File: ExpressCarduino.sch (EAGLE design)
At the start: 1 part

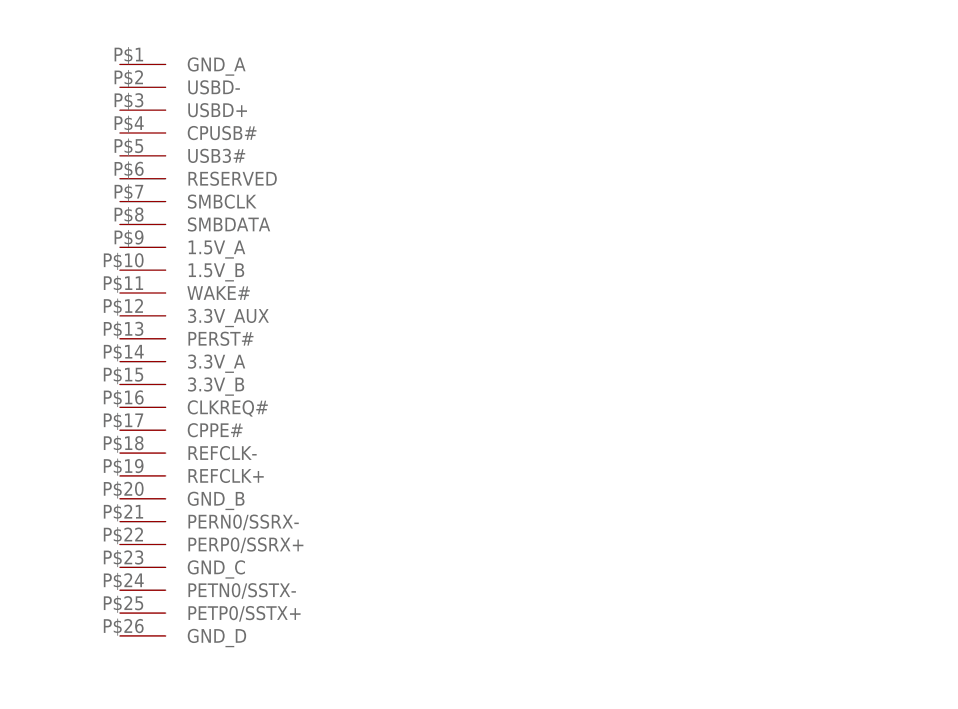
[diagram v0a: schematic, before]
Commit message: Added vreg circuit for 3.3v -> 9v and images
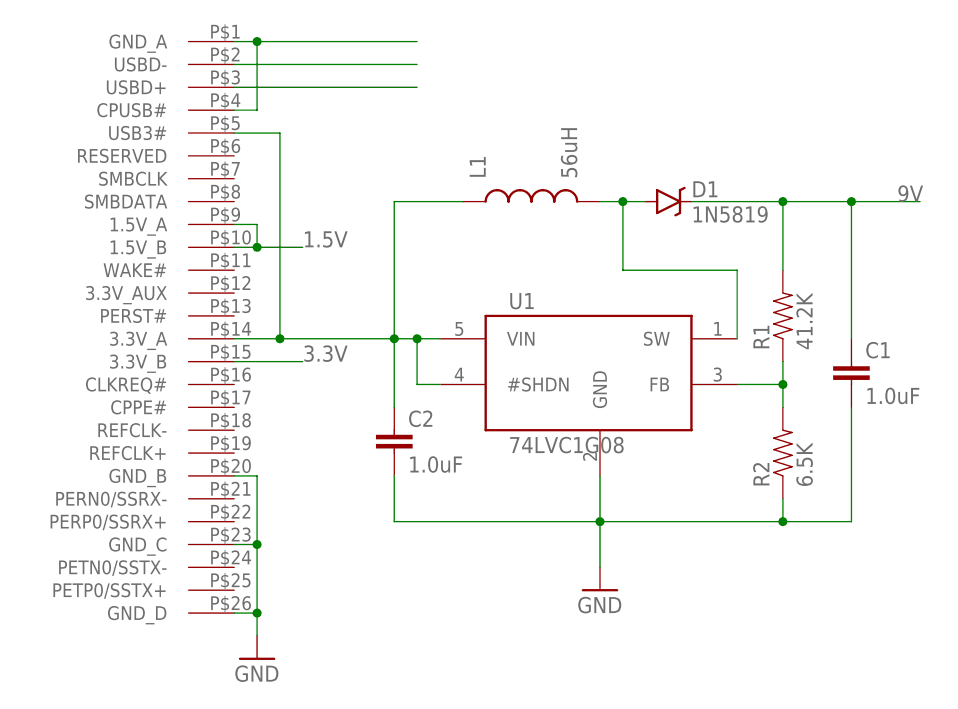
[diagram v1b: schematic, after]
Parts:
- added C1, C2: 1.0uF, SparkFun-Capacitors:1.0UF-16V-10%(0603)
- added D1: 1N5819, HokieGeek:DIODE-SCHOTTKY
- added L1: 56uH, SparkFun-Passives:INDUCTORSDR0403-560KL
- added R1: 41.2K, SparkFun-Resistors:0.22OHM-1/4W-1%(0805)
- added R2: 6.5K, SparkFun-Resistors:0.22OHM-1/4W-1%(0805)
- added U1: 74LVC1G08, HokieGeek:AP3012
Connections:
- new net 1.5V: U$1.1.5V_A, U$1.1.5V_B
- new net 3.3V: U$1.3.3V_B
- new net 9V: C1.1, D1.C, R1.2
- new net GND: C1.2, C2.2, R2.1, U$1.CPUSB#, U$1.GND_A, U$1.GND_B, U$1.GND_C, U$1.GND_D, U1.GND
- new net N$1: R1.1, R2.2, U1.FB
- new net N$2: C2.1, L1.1, U$1.3.3V_A, U$1.USB3#, U1.#SHDN, U1.VIN
- new net N$3: D1.A, L1.2, U1.SW
- new net N$4: U$1.USBD-
- new net N$5: U$1.USBD+

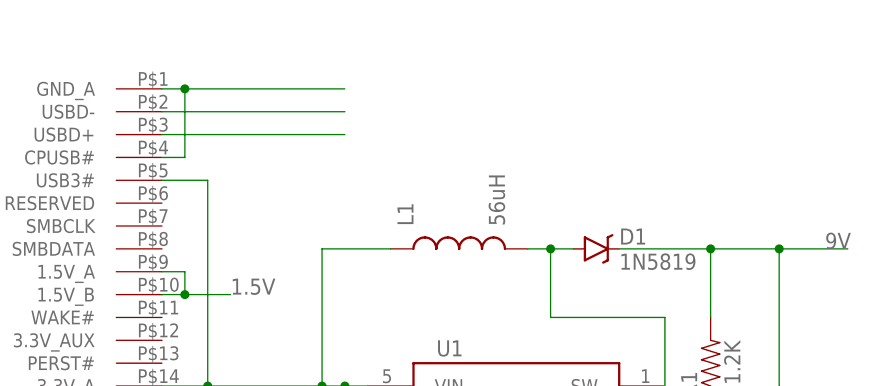
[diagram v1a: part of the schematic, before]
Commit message: Added the Mini USB part
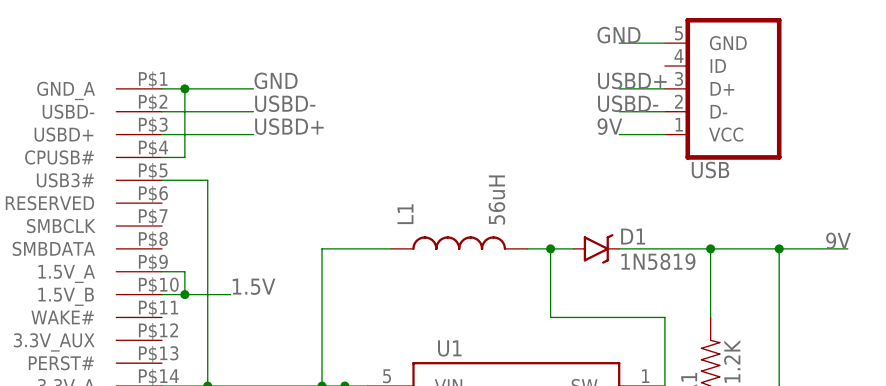
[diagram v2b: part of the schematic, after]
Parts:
- added USB: (no value), HokieGeek:USB_MICROB_PLUG"
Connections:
- removed net N$4: U$1.USBD-
- removed net N$5: U$1.USBD+
- new net USBD+: U$1.USBD+, USB.D+
- new net USBD-: U$1.USBD-, USB.D-
- net 9V: now also USB.VCC
- net GND: now also USB.GND
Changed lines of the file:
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@@
 <part name="L1" library="SparkFun-Passives" deviceset="INDUCTOR" device="SDR0403-560KL" value="56uH"/>
 <part name="D1" library="HokieGeek" deviceset="DIODE-SCHOTTKY" device="" value="1N5819"/>
+<part name="USB" library="HokieGeek" deviceset="USB_MICROB_PLUG" device="&quot;"/>
 </parts>
 <sheets>
@@
 <instance part="L1" gate="G$1" x="48.26" y="50.8" rot="R90"/>
 <instance part="D1" gate="G$1" x="63.5" y="50.8"/>
+<instance part="USB" gate="G$1" x="78.74" y="68.58" rot="MR180"/>
 </instances>
 <busses>
@@
 </segment>
 </net>
-<net name="N$4" class="0">
+<net name="USBD-" class="0">
 <segment>
 <pinref part="U$1" gate="G$1" pin="USBD-"/>
-<wire x1="15.24" y1="66.04" x2="35.56" y2="66.04" width="0.1524" layer="91"/>
+<wire x1="15.24" y1="66.04" x2="25.4" y2="66.04" width="0.1524" layer="91"/>
+<label x="25.4" y="66.04" size="1.778" layer="95"/>
+</segment>
+<segment>
+<pinref part="USB" gate="G$1" pin="D-"/>
+<wire x1="71.12" y1="66.04" x2="66.04" y2="66.04" width="0.1524" layer="91"/>
+<label x="63.5" y="66.04" size="1.778" layer="95"/>
 </segment>
 </net>
-<net name="N$5" class="0">
+<net name="USBD+" class="0">
 <segment>
 <pinref part="U$1" gate="G$1" pin="USBD+"/>
-<wire x1="15.24" y1="63.5" x2="35.56" y2="63.5" width="0.1524" layer="91"/>
+<wire x1="15.24" y1="63.5" x2="25.4" y2="63.5" width="0.1524" layer="91"/>
+<label x="25.4" y="63.5" size="1.778" layer="95"/>
+</segment>
+<segment>
+<pinref part="USB" gate="G$1" pin="D+"/>
+<wire x1="71.12" y1="68.58" x2="66.04" y2="68.58" width="0.1524" layer="91"/>
+<label x="63.5" y="68.58" size="1.778" layer="95"/>
 </segment>
 </net>
@@
 <pinref part="U$1" gate="G$1" pin="GND_A"/>
 <wire x1="15.24" y1="68.58" x2="17.78" y2="68.58" width="0.1524" layer="91"/>
-<wire x1="17.78" y1="68.58" x2="35.56" y2="68.58" width="0.1524" layer="91"/>
+<wire x1="17.78" y1="68.58" x2="25.4" y2="68.58" width="0.1524" layer="91"/>
 <wire x1="17.78" y1="60.96" x2="17.78" y2="68.58" width="0.1524" layer="91"/>
 <junction x="17.78" y="68.58"/>
+<label x="25.4" y="68.58" size="1.778" layer="95"/>
 </segment>
 <segment>
@@
 <wire x1="55.88" y1="15.24" x2="33.02" y2="15.24" width="0.1524" layer="91"/>
 <wire x1="33.02" y1="15.24" x2="33.02" y2="20.32" width="0.1524" layer="91"/>
+</segment>
+<segment>
+<pinref part="USB" gate="G$1" pin="GND"/>
+<wire x1="71.12" y1="73.66" x2="66.04" y2="73.66" width="0.1524" layer="91"/>
+<label x="63.5" y="73.66" size="1.778" layer="95"/>
 </segment>
 </net>
@@
 <label x="88.9" y="50.8" size="1.778" layer="95"/>
 </segment>
+<segment>
+<pinref part="USB" gate="G$1" pin="VCC"/>
+<wire x1="71.12" y1="63.5" x2="66.04" y2="63.5" width="0.1524" layer="91"/>
+<label x="63.5" y="63.5" size="1.778" layer="95"/>
+</segment>
 </net>

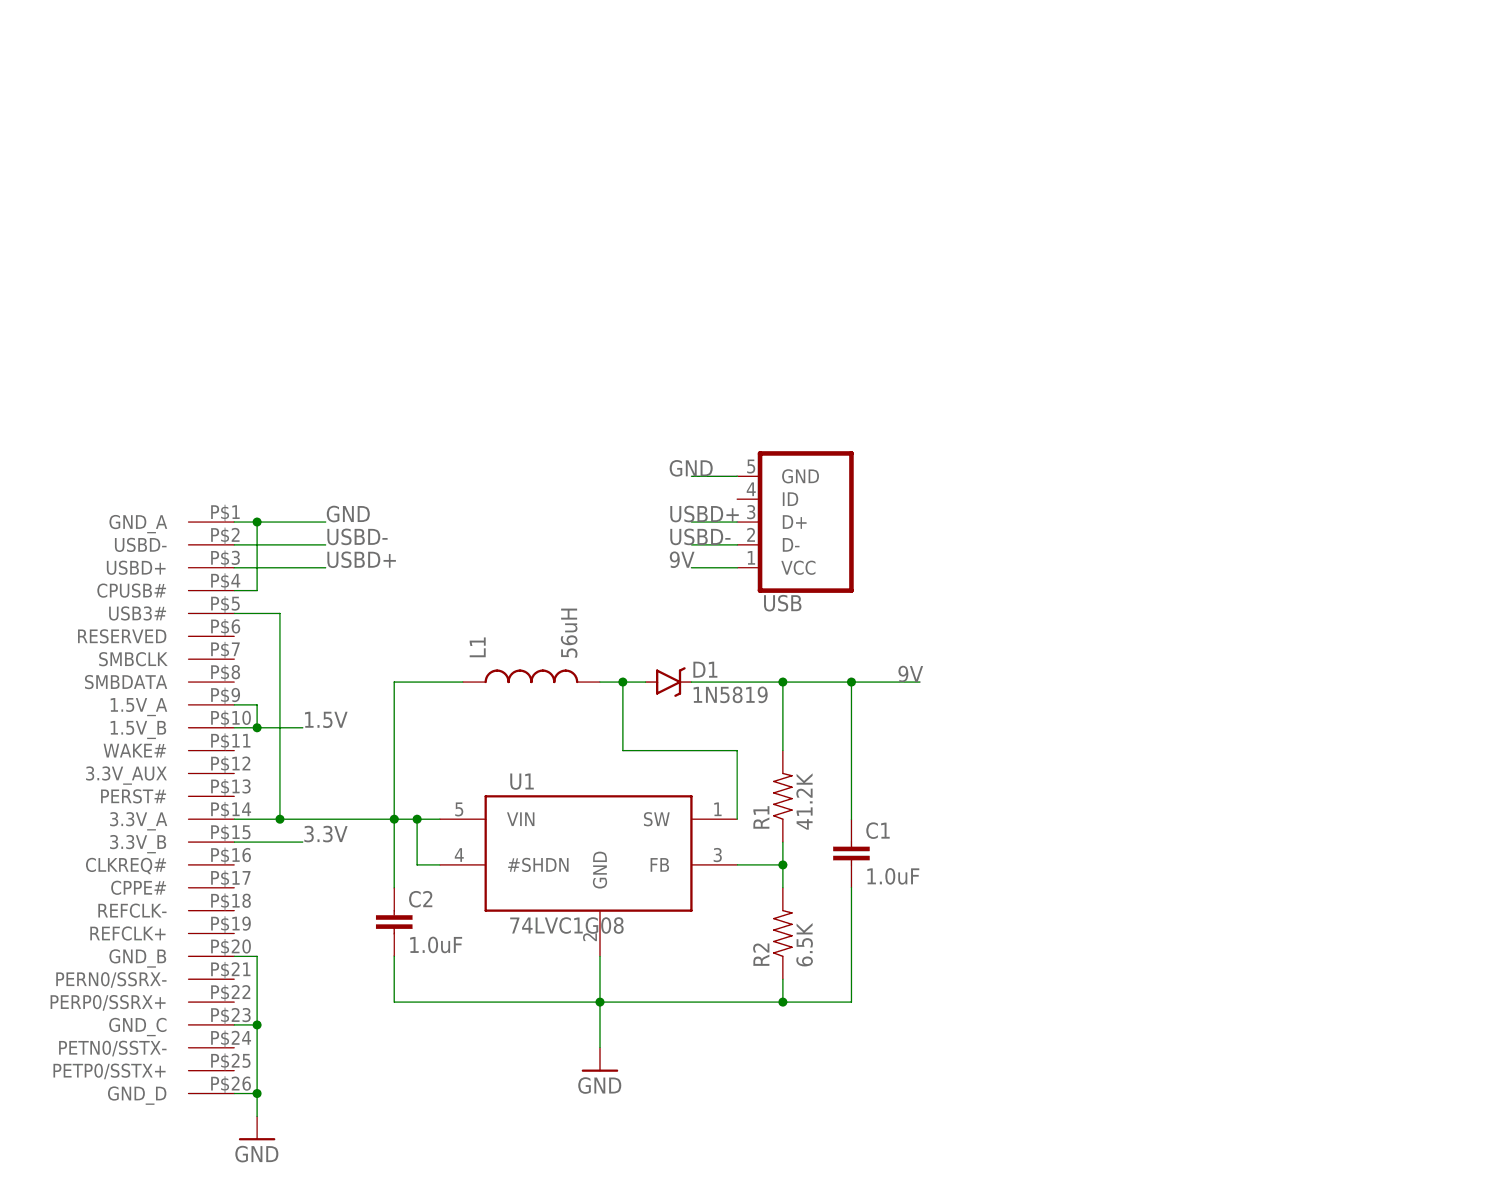
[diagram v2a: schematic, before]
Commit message: Added an IO expander and more ADC lines. Not sure why, tbh
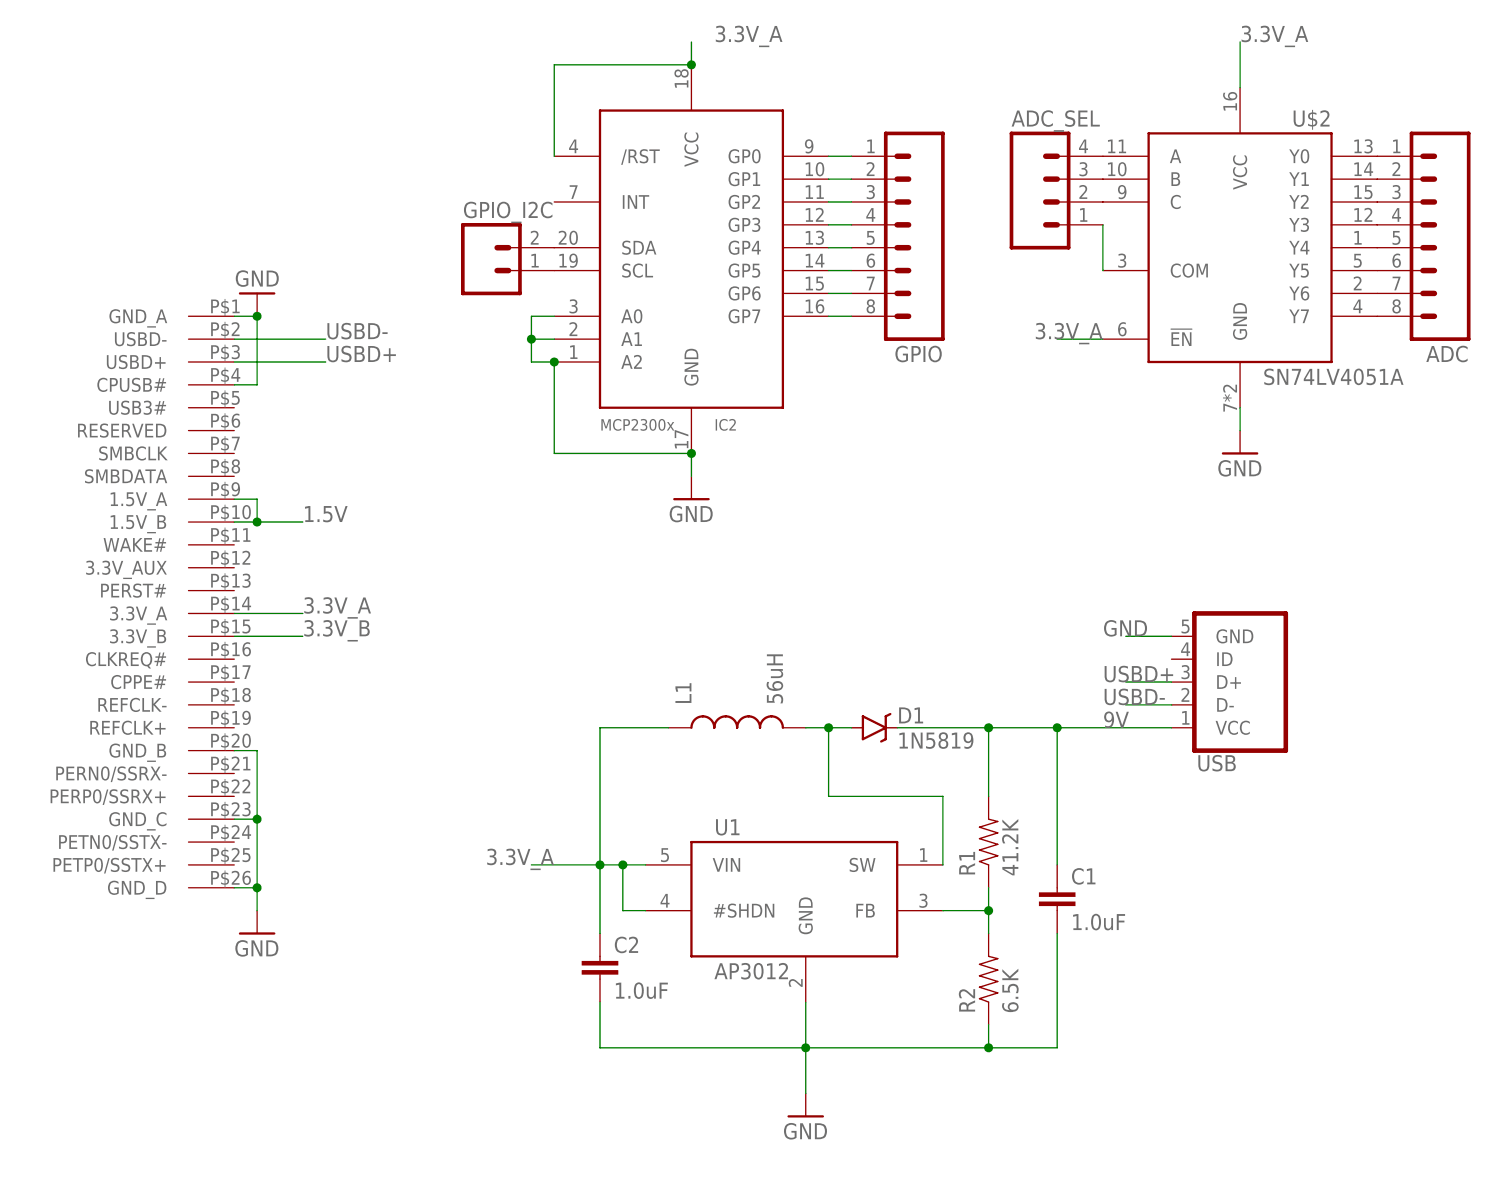
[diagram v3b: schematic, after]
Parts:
- added ADC, GPIO: (no value), SparkFun-Connectors:M08
- added ADC_SEL: (no value), SparkFun-Connectors:M04PTH
- added GPIO_I2C: (no value), SparkFun-Connectors:M02PTH
- added IC2: MCP23008, HokieGeek:MCP23008
- added U$2: SN74LV4051A, HokieGeek:SN74LV4051A
- U1: value 74LVC1G08 -> AP3012
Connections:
- net 3.3V renamed 3.3V_B
- new net 3.3V_A: C2.1, IC2./RST, IC2.VCC, L1.1, U$1.3.3V_A, U$2.!EN, U$2.VCC, U1.#SHDN, U1.VIN
- new net N$10: GPIO.8, IC2.GP7
- new net N$11: GPIO_I2C.1, IC2.SCL
- new net N$12: GPIO_I2C.2, IC2.SDA
- new net N$13: ADC_SEL.1, U$2.COM
- new net N$19: ADC.1, U$2.Y0
- new net N$20: ADC.2, U$2.Y1
- new net N$21: ADC.3, U$2.Y2
- new net N$22: ADC.4, U$2.Y3
- new net N$23: ADC.5, U$2.Y4
- new net N$24: ADC.6, U$2.Y5
- new net N$25: ADC.7, U$2.Y6
- new net N$26: ADC.8, U$2.Y7
- new net N$29: ADC_SEL.2, U$2.C
- new net N$30: ADC_SEL.3, U$2.B
- new net N$31: ADC_SEL.4, U$2.A
- new net N$4: GPIO.2, IC2.GP1
- new net N$5: GPIO.3, IC2.GP2
- new net N$6: GPIO.4, IC2.GP3
- new net N$7: GPIO.5, IC2.GP4
- new net N$8: GPIO.6, IC2.GP5
- new net N$9: GPIO.7, IC2.GP6
- net GND: now also IC2.A0, IC2.A1, IC2.A2, IC2.GND, U$2.GND
- net N$2: now also GPIO.1, IC2.GP0; no longer C2.1, L1.1, U$1.3.3V_A, U$1.USB3#, U1.#SHDN, U1.VIN
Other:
- moved on the sheet: C1, C2, D1, L1, R1, R2, U1, USB
